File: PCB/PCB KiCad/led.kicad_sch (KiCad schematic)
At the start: 22 parts, among them U5 TLC59208FIPWR

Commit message: export for review
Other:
- company: (none) -> Plastic Scanner
- title: (none) -> Development Board
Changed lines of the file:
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@@
 (kicad_sch (version 20211123) (generator eeschema)
   (paper "A4")
+  (title_block
+    (title "Development Board")
+    (date "2022-03-15")
+    (rev "2.1")
+    (company "Plastic Scanner")
+  )
   (junction (at 208.28 110.49) (diameter 0) (color 0 0 0 0)
   )

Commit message: PCB at time of order
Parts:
- renumbered C17 to C18
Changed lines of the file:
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@@
   (symbol (lib_id "power:GND") (at 130.81 102.87 0) (unit 1)
     (in_bom yes) (on_board yes) (fields_autoplaced)
-    (property "Reference" "#PWR036" (id 0) (at 130.81 109.22 0)
+    (property "Reference" "#PWR037" (id 0) (at 130.81 109.22 0)
       (effects (font (size 1.27 1.27)) hide)
     )
@@
   (symbol (lib_id "Device:C") (at 123.19 124.46 0) (unit 1)
     (in_bom yes) (on_board yes) (fields_autoplaced)
-    (property "Reference" "C17" (id 0) (at 127 123.1899 0)
+    (property "Reference" "C18" (id 0) (at 127 123.1899 0)
       (effects (font (size 1.27 1.27)) (justify left))
     )
@@
   (symbol (lib_id "power:GND") (at 166.37 137.16 0) (unit 1)
     (in_bom yes) (on_board yes) (fields_autoplaced)
-    (property "Reference" "#PWR037" (id 0) (at 166.37 143.51 0)
+    (property "Reference" "#PWR038" (id 0) (at 166.37 143.51 0)
       (effects (font (size 1.27 1.27)) hide)
     )
@@
   (symbol (lib_id "power:GND") (at 123.19 130.175 0) (unit 1)
     (in_bom yes) (on_board yes) (fields_autoplaced)
-    (property "Reference" "#PWR035" (id 0) (at 123.19 136.525 0)
+    (property "Reference" "#PWR036" (id 0) (at 123.19 136.525 0)
       (effects (font (size 1.27 1.27)) hide)
     )
@@
   (symbol (lib_id "power:+3.3V") (at 208.28 41.275 0) (unit 1)
     (in_bom yes) (on_board yes) (fields_autoplaced)
-    (property "Reference" "#PWR038" (id 0) (at 208.28 45.085 0)
+    (property "Reference" "#PWR039" (id 0) (at 208.28 45.085 0)
       (effects (font (size 1.27 1.27)) hide)
     )
@@
   (symbol (lib_id "power:+3.3V") (at 123.19 67.31 0) (unit 1)
     (in_bom yes) (on_board yes) (fields_autoplaced)
-    (property "Reference" "#PWR034" (id 0) (at 123.19 71.12 0)
-      (effects (font (size 1.27 1.27)) hide)
-    )
+    (property "Reference" "#PWR035" (id 0) (at 123.19 71.12 0)
+      (effects (font (size 1.27 1.27)) hide)
+    )

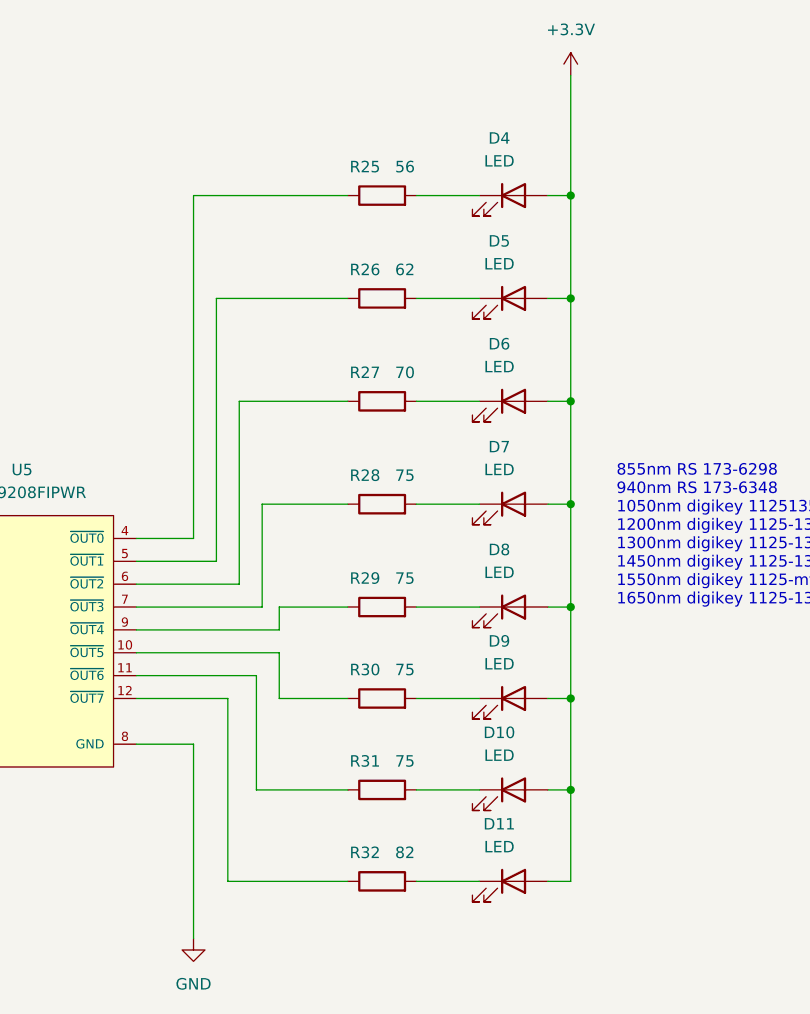
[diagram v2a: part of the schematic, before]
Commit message: Adds 1720nm datasheet and corrects some typ's
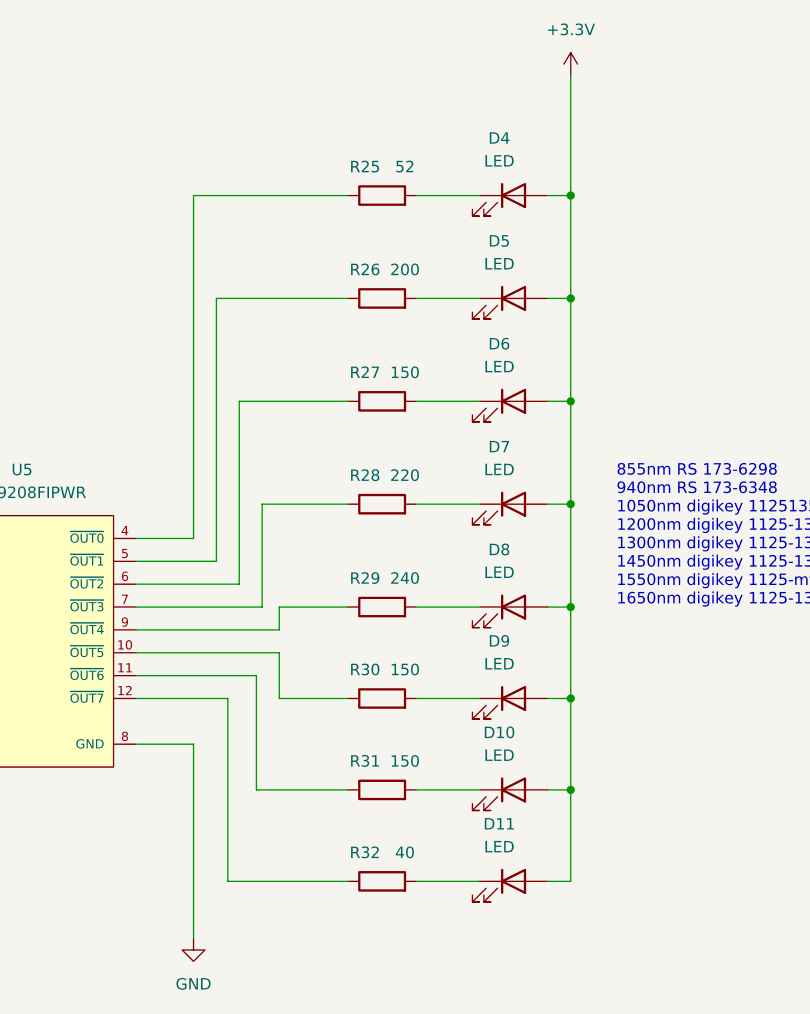
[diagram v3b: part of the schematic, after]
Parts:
- R25: value 56 -> 52
- R26: value 62 -> 200
- R27: value 70 -> 150
- R28: value 75 -> 220
- R29: value 75 -> 240
- R30, R31: value 75 -> 150
- R32: value 82 -> 40
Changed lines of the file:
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@@
     (in_bom yes) (on_board yes)
     (property "Reference" "R32" (id 0) (at 185.42 127.635 90))
-    (property "Value" "82" (id 1) (at 189.865 127.635 90))
+    (property "Value" "40" (id 1) (at 189.865 127.635 90))
     (property "Footprint" "Resistor_SMD:R_0805_2012Metric_Pad1.20x1.40mm_HandSolder" (id 2) (at 187.325 132.588 90)
       (effects (font (size 1.27 1.27)) hide)
@@
     (in_bom yes) (on_board yes)
     (property "Reference" "R26" (id 0) (at 185.42 62.865 90))
-    (property "Value" "62" (id 1) (at 189.865 62.865 90))
+    (property "Value" "200" (id 1) (at 189.865 62.865 90))
     (property "Footprint" "Resistor_SMD:R_0805_2012Metric_Pad1.20x1.40mm_HandSolder" (id 2) (at 187.325 67.818 90)
       (effects (font (size 1.27 1.27)) hide)
@@
     (in_bom yes) (on_board yes)
     (property "Reference" "R25" (id 0) (at 185.42 51.435 90))
-    (property "Value" "56" (id 1) (at 189.865 51.435 90))
+    (property "Value" "52" (id 1) (at 189.865 51.435 90))
     (property "Footprint" "Resistor_SMD:R_0805_2012Metric_Pad1.20x1.40mm_HandSolder" (id 2) (at 187.325 56.388 90)
       (effects (font (size 1.27 1.27)) hide)
@@
     (in_bom yes) (on_board yes)
     (property "Reference" "R30" (id 0) (at 185.42 107.315 90))
-    (property "Value" "75" (id 1) (at 189.865 107.315 90))
+    (property "Value" "150" (id 1) (at 189.865 107.315 90))
     (property "Footprint" "Resistor_SMD:R_0805_2012Metric_Pad1.20x1.40mm_HandSolder" (id 2) (at 187.325 112.268 90)
       (effects (font (size 1.27 1.27)) hide)
@@
     (in_bom yes) (on_board yes)
     (property "Reference" "R29" (id 0) (at 185.42 97.155 90))
-    (property "Value" "75" (id 1) (at 189.865 97.155 90))
+    (property "Value" "240" (id 1) (at 189.865 97.155 90))
     (property "Footprint" "Resistor_SMD:R_0805_2012Metric_Pad1.20x1.40mm_HandSolder" (id 2) (at 187.325 102.108 90)
       (effects (font (size 1.27 1.27)) hide)
@@
     (in_bom yes) (on_board yes)
     (property "Reference" "R31" (id 0) (at 185.42 117.475 90))
-    (property "Value" "75" (id 1) (at 189.865 117.475 90))
+    (property "Value" "150" (id 1) (at 189.865 117.475 90))
     (property "Footprint" "Resistor_SMD:R_0805_2012Metric_Pad1.20x1.40mm_HandSolder" (id 2) (at 187.325 122.428 90)
       (effects (font (size 1.27 1.27)) hide)
@@
     (in_bom yes) (on_board yes)
     (property "Reference" "R27" (id 0) (at 185.42 74.295 90))
-    (property "Value" "70" (id 1) (at 189.865 74.295 90))
+    (property "Value" "150" (id 1) (at 189.865 74.295 90))
     (property "Footprint" "Resistor_SMD:R_0805_2012Metric_Pad1.20x1.40mm_HandSolder" (id 2) (at 187.325 79.248 90)
       (effects (font (size 1.27 1.27)) hide)
@@
     (in_bom yes) (on_board yes)
     (property "Reference" "R28" (id 0) (at 185.42 85.725 90))
-    (property "Value" "75" (id 1) (at 189.865 85.725 90))
+    (property "Value" "220" (id 1) (at 189.865 85.725 90))
     (property "Footprint" "Resistor_SMD:R_0805_2012Metric_Pad1.20x1.40mm_HandSolder" (id 2) (at 187.325 90.678 90)
       (effects (font (size 1.27 1.27)) hide)

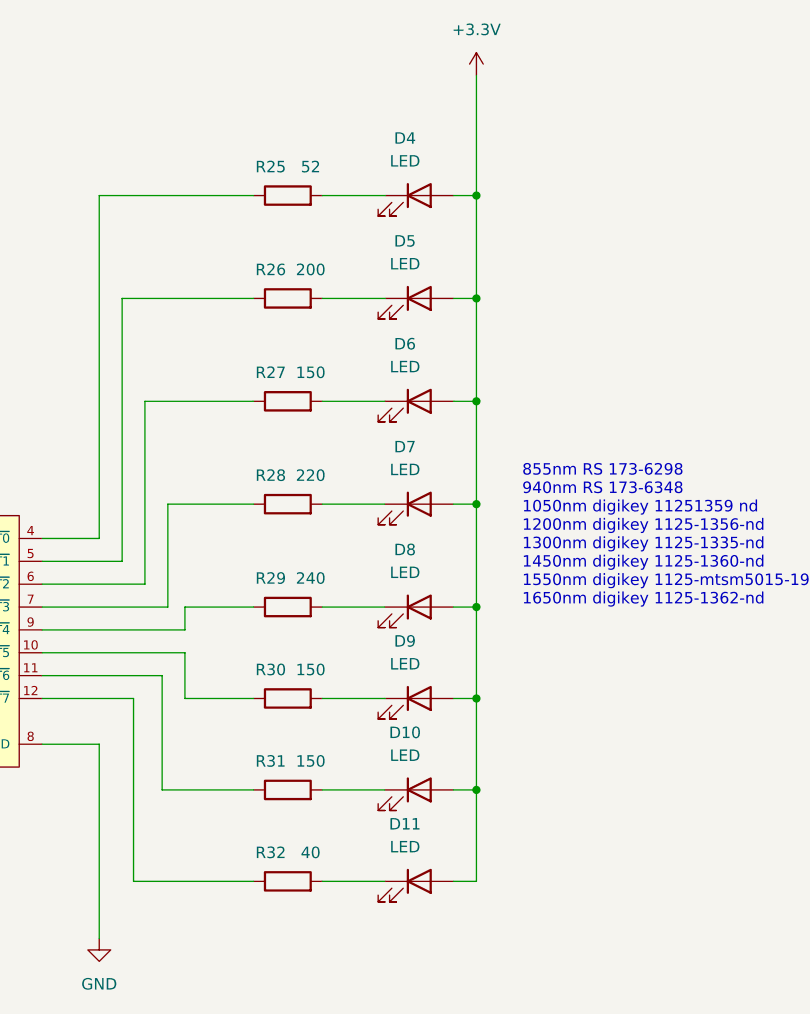
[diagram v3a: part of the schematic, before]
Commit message: adds wavelengths to BOM
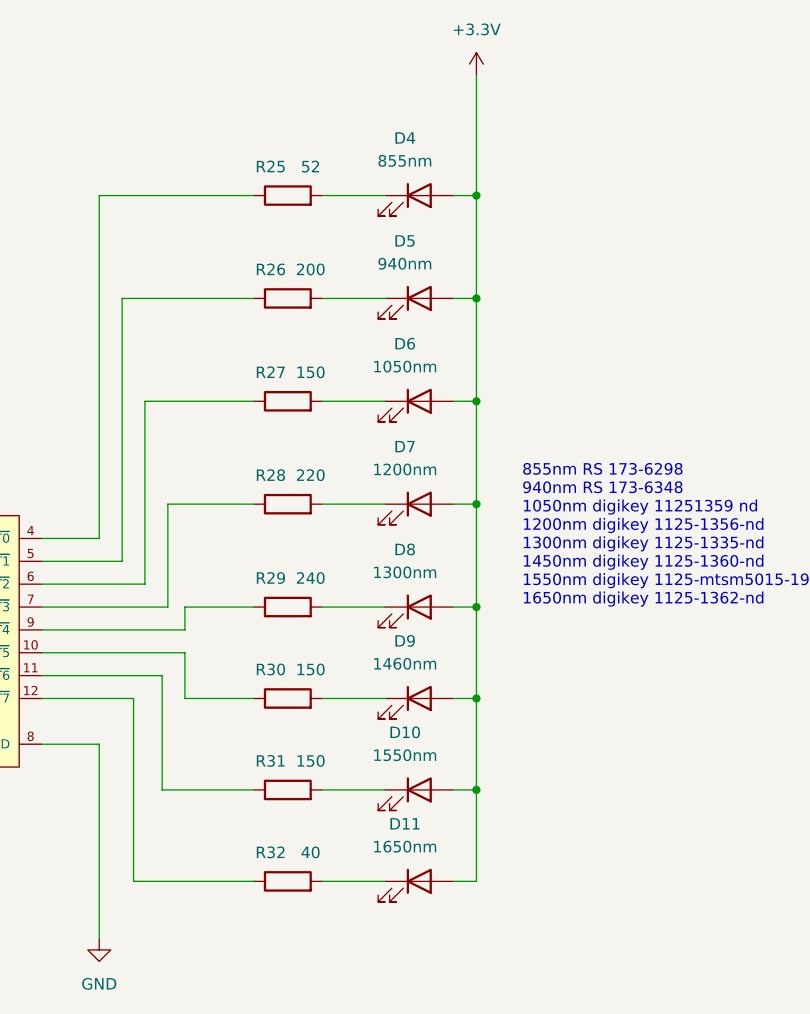
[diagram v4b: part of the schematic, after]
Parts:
- D10: value LED -> 1550nm
- D11: value LED -> 1650nm
- D4: value LED -> 855nm
- D5: value LED -> 940nm
- D6: value LED -> 1050nm
- D7: value LED -> 1200nm
- D8: value LED -> 1300nm
- D9: value LED -> 1460nm
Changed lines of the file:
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@@
     (in_bom yes) (on_board yes) (fields_autoplaced)
     (property "Reference" "D8" (id 0) (at 200.3425 93.98 0))
-    (property "Value" "LED" (id 1) (at 200.3425 96.52 0))
+    (property "Value" "1300nm" (id 1) (at 200.3425 96.52 0))
     (property "Footprint" "LED_SMD:LED_1206_3216Metric_Pad1.42x1.75mm_HandSolder" (id 2) (at 201.93 100.33 0)
       (effects (font (size 1.27 1.27)) hide)
     )
-    (property "Datasheet" "~" (id 3) (at 201.93 100.33 0)
+    (property "Datasheet" "https://marktechopto.com/pdf/products/DataSheet/MTSM0013-844-IR.pdf" (id 3) (at 201.93 100.33 0)
       (effects (font (size 1.27 1.27)) hide)
     )
@@
     (in_bom yes) (on_board yes) (fields_autoplaced)
     (property "Reference" "D9" (id 0) (at 200.3425 104.14 0))
-    (property "Value" "LED" (id 1) (at 200.3425 106.68 0))
+    (property "Value" "1460nm" (id 1) (at 200.3425 106.68 0))
     (property "Footprint" "LED_SMD:LED_1206_3216Metric_Pad1.42x1.75mm_HandSolder" (id 2) (at 201.93 110.49 0)
       (effects (font (size 1.27 1.27)) hide)
     )
-    (property "Datasheet" "~" (id 3) (at 201.93 110.49 0)
+    (property "Datasheet" "https://marktechopto.com/pdf/products/datasheet/MTSM6014-844-IR.pdf" (id 3) (at 201.93 110.49 0)
       (effects (font (size 1.27 1.27)) hide)
     )
@@
     (in_bom yes) (on_board yes) (fields_autoplaced)
     (property "Reference" "D4" (id 0) (at 200.3425 48.26 0))
-    (property "Value" "LED" (id 1) (at 200.3425 50.8 0))
+    (property "Value" "855nm" (id 1) (at 200.3425 50.8 0))
     (property "Footprint" "LED_SMD:LED_1206_3216Metric_Pad1.42x1.75mm_HandSolder" (id 2) (at 201.93 54.61 0)
       (effects (font (size 1.27 1.27)) hide)
     )
-    (property "Datasheet" "~" (id 3) (at 201.93 54.61 0)
+    (property "Datasheet" "https://nl.rs-online.com/web/p/ir-leds/1736298/" (id 3) (at 201.93 54.61 0)
       (effects (font (size 1.27 1.27)) hide)
     )
@@
     (in_bom yes) (on_board yes) (fields_autoplaced)
     (property "Reference" "D7" (id 0) (at 200.3425 82.55 0))
-    (property "Value" "LED" (id 1) (at 200.3425 85.09 0))
+    (property "Value" "1200nm" (id 1) (at 200.3425 85.09 0))
     (property "Footprint" "LED_SMD:LED_1206_3216Metric_Pad1.42x1.75mm_HandSolder" (id 2) (at 201.93 88.9 0)
       (effects (font (size 1.27 1.27)) hide)
     )
-    (property "Datasheet" "~" (id 3) (at 201.93 88.9 0)
+    (property "Datasheet" "https://www.marktechopto.com/pdf/products/datasheet/MTSM0012-843-IR.pdf" (id 3) (at 201.93 88.9 0)
       (effects (font (size 1.27 1.27)) hide)
     )
@@
     (in_bom yes) (on_board yes) (fields_autoplaced)
     (property "Reference" "D11" (id 0) (at 200.3425 124.46 0))
-    (property "Value" "LED" (id 1) (at 200.3425 127 0))
+    (property "Value" "1650nm" (id 1) (at 200.3425 127 0))
     (property "Footprint" "LED_SMD:LED_1206_3216Metric_Pad1.42x1.75mm_HandSolder" (id 2) (at 201.93 130.81 0)
       (effects (font (size 1.27 1.27)) hide)
     )
-    (property "Datasheet" "~" (id 3) (at 201.93 130.81 0)
+    (property "Datasheet" "https://www.marktechopto.com/pdf/products/datasheet/MTSM5016-843-IR.pdf" (id 3) (at 201.93 130.81 0)
       (effects (font (size 1.27 1.27)) hide)
     )
@@
     (in_bom yes) (on_board yes) (fields_autoplaced)
     (property "Reference" "D6" (id 0) (at 200.3425 71.12 0))
-    (property "Value" "LED" (id 1) (at 200.3425 73.66 0))
+    (property "Value" "1050nm" (id 1) (at 200.3425 73.66 0))
     (property "Footprint" "LED_SMD:LED_1206_3216Metric_Pad1.42x1.75mm_HandSolder" (id 2) (at 201.93 77.47 0)
       (effects (font (size 1.27 1.27)) hide)
     )
-    (property "Datasheet" "~" (id 3) (at 201.93 77.47 0)
+    (property "Datasheet" "https://www.marktechopto.com/pdf/products/datasheet/MTSM5010-843-IR.pdf" (id 3) (at 201.93 77.47 0)
       (effects (font (size 1.27 1.27)) hide)
     )
@@
     (in_bom yes) (on_board yes) (fields_autoplaced)
     (property "Reference" "D5" (id 0) (at 200.3425 59.69 0))
-    (property "Value" "LED" (id 1) (at 200.3425 62.23 0))
+    (property "Value" "940nm" (id 1) (at 200.3425 62.23 0))
     (property "Footprint" "LED_SMD:LED_1206_3216Metric_Pad1.42x1.75mm_HandSolder" (id 2) (at 201.93 66.04 0)
       (effects (font (size 1.27 1.27)) hide)
     )
-    (property "Datasheet" "~" (id 3) (at 201.93 66.04 0)
+    (property "Datasheet" "https://nl.rs-online.com/web/p/ir-leds/1736348" (id 3) (at 201.93 66.04 0)
       (effects (font (size 1.27 1.27)) hide)
     )
@@
     (in_bom yes) (on_board yes) (fields_autoplaced)
     (property "Reference" "D10" (id 0) (at 200.3425 114.3 0))
-    (property "Value" "LED" (id 1) (at 200.3425 116.84 0))
+    (property "Value" "1550nm" (id 1) (at 200.3425 116.84 0))
     (property "Footprint" "LED_SMD:LED_1206_3216Metric_Pad1.42x1.75mm_HandSolder" (id 2) (at 201.93 120.65 0)
       (effects (font (size 1.27 1.27)) hide)
     )
-    (property "Datasheet" "~" (id 3) (at 201.93 120.65 0)
-      (effects (font (size 1.27 1.27)) hide)
-    )
+    (property "Datasheet" "https://marktechopto.com/pdf/products/DataSheet/MTSM5015-844-IR,.pdf" (id 3) (at 201.93 120.65 0)
+      (effects (font (size 1.27 1.27)) hide)
+    )
